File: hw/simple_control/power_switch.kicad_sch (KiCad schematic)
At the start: 0 parts

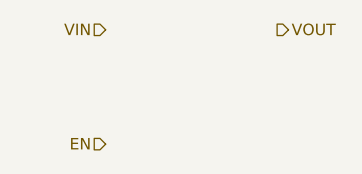
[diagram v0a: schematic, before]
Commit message: [hw] Complete root schematics of simple control
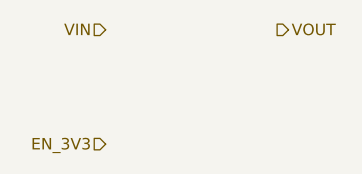
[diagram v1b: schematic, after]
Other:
- company: (none) -> Stefan Misik
- title: (none) -> WS2812 Simple Controller
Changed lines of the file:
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@@
 (kicad_sch (version 20230121) (generator eeschema)
   (paper "A4")
+  (title_block
+    (title "WS2812 Simple Controller")
+    (date "2023-03-09")
+    (company "Stefan Misik")
+  )
   (hierarchical_label "VOUT" (shape output) (at 95.25 88.9 0) (fields_autoplaced)
     (effects (font (size 1.27 1.27)) (justify left))
@@
     (effects (font (size 1.27 1.27)) (justify right))
   )
-  (hierarchical_label "EN" (shape input) (at 76.2 101.6 180) (fields_autoplaced)
+  (hierarchical_label "EN_3V3" (shape input) (at 76.2 101.6 180) (fields_autoplaced)
     (effects (font (size 1.27 1.27)) (justify right))
   )

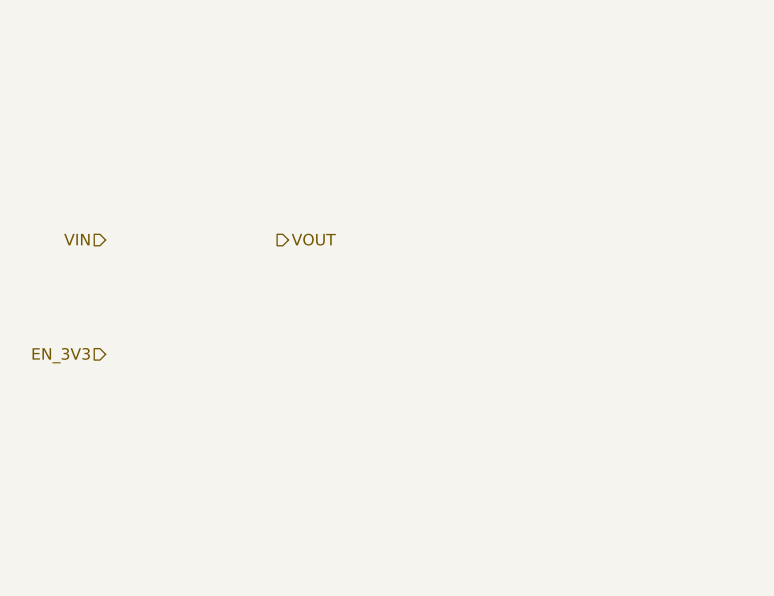
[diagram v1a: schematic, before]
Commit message: [hw] Add simple power switch circuit
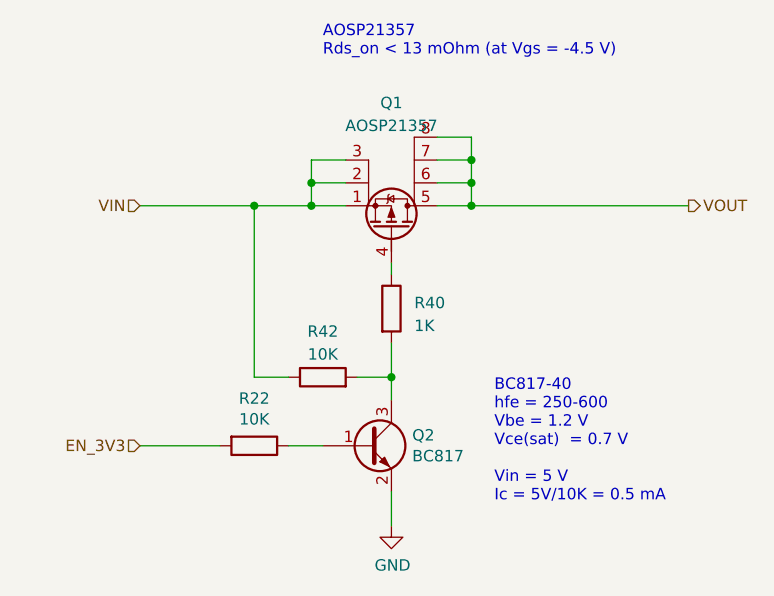
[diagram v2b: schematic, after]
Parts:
- added Q1: AOSP21357, symbol my:Q_PMOS_SSSGDDDD
- added Q2: BC817, Package_TO_SOT_SMD:SOT-23_Handsoldering, symbol Device:Q_NPN_BEC
- added R22: 10K, Resistor_SMD:R_0805_2012Metric_Pad1.20x1.40mm_HandSolder, symbol Device:R
- added R40: 1K, symbol Device:R
- added R42: 10K, symbol Device:R
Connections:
- net EN_3V3: now also R22.2
- net VIN: now also Q1.1 (S), Q1.2 (S), Q1.3 (S), R42.1
- net VOUT: now also Q1.5 (D), Q1.6 (D), Q1.7 (D), Q1.8 (D)
- new net: Q1.4 (G), R40.1
- new net: Q2.1 (B), R22.1
- new net: Q2.3 (C), R40.2, R42.2
- new net GND: Q2.2 (E)
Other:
- note added: "AOSP21357 Rds_on < 13 mOhm (at Vgs = -4.5 V)"
- note added: "BC817-40 hfe = 250-600 Vbe = 1.2 V Vce(sat) = 0.7 V Vin = 5 V Ic = 5V/10K = 0.5 mA"
